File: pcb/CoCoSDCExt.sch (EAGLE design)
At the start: 47 parts, among them IC1 AM29F040J, IC2 XC9572XLVQG64, IC3 YM2413R, IC4 SN76489R, IC6 LM4558D, X1 EXPANSION_PORT_COCO, X2 EXPANSION_PORT_COCOS

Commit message: Add in YMF-262 audio IC
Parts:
- added C4.4: 50p, rcl:C-USC0402
- added C4.5, C4.6: 2n7, rcl:C-USC0402
- added C7: 10, rcl:CPOL-US140CLH-0810
- added IC10: YAC512-M, yamaha:YAC512-M
- added IC14, IC15: TL072D, linear:TL072D
- added IC9: YMF262-M, yamaha:YMF262-M
- added OSC2: 16MHz, crystal:ASE
- added R9: 33, resistor:R-US_R1206
- added U$1: (no value), coco:PROGRAM_PAK
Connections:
- new net !CE_YMF262: IC9A.!CS
- new net !IRQ_AUDIO: IC9A.!IRQ
- new net !OE: IC9A.!RD
- new net !RESET_AUDIO: IC9A.!IC
- new net AB0: IC9A.A0
- new net AB1: IC9A.A1
- new net DB0: IC9A.D0
- new net DB1: IC9A.D1
- new net DB2: IC9A.D2
- new net DB3: IC9A.D3
- new net DB4: IC9A.D4
- new net DB5: IC9A.D5
- new net DB6: IC9A.D6
- new net DB7: IC9A.D7
- new net N$10: IC10A.SMP1, IC9A.SMPAC
- new net N$11: IC10A.SMP2, IC9A.SMPBD
- new net N$12: IC9A.CLK, OSC2.OUT
- new net N$14: IC10A.SWIN, R9.2
- new net N$18: IC15B.-IN, IC15B.OUT, R9.1
- new net N$19: C4.6.1, IC10A.CH1, IC14B.+IN
- new net N$20: C4.5.1, IC10A.CH2, IC14A.+IN
- new net N$23: C4.4.1, IC10A.AOUT, IC15B.+IN
- new net N$26: IC10A.MP, IC15A.-IN, IC15A.OUT
- new net N$28: C7.+, IC10A.CV, IC15A.+IN
- new net N$6: IC10A.CLK, IC9A.SY
- new net N$7: IC10A.DIN, IC9A.DOAB
- new net YMF_CH_0: IC14B.-IN, IC14B.OUT
- new net YMF_CH_1: IC14A.-IN, IC14A.OUT
- net !WE: now also IC9A.!WR
- net +3V3: now also OSC2.VDD
- net +5V: now also IC10A.FSEL, IC10A.TEST1
- net GND: now also C4.4.2, C4.5.2, C4.6.2, C7.-, OSC2.GND

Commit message: Initial fitment
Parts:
- removed C1.2, C3.1, C4.1: .1, resistor:C-USC0402
- removed C10, C11, C2: .1, resistor:C-EUC1206
- removed C14, C16, C3: .0015, resistor:C-EUC1206
- removed C4: 10, resistor:C-USC0805
- removed C5: 1/50, resistor:C-USC0805
- removed IC3: YM2413R, yamaha:YM2413R
- removed IC4: SN76489R, texas-instruments:SN76489R
- removed IC6: LM4558D, op-amps-jlb:LM4558D
- removed OSC2: 16MHz, crystal:ASE
- removed R1: 10K, resistor:R-US_R0402
- removed R2, R38, R39: 10K, rcl:R-US_R1206
- removed R3, R4, R5: 4K7, rcl:R-US_R1206
- removed R40: 16K, rcl:R-US_R1206
- removed R41: 1.3K (1%), rcl:R-US_R0402
- removed R42: 1k (1%), rcl:R-US_R0402
- removed R6, R7, R8: 2K2, rcl:R-US_R1206
- added C10.1, C14.1, C15.1, C15.2, C9.1: .1, rcl:C-USC0402
- added C17, C18, C19, C20: (no value), cap-pan40:C-BP-SMD-SV-B
- added C4.2: 10u, rcl:C-USC0402
- added R10, R11: 2K, resistor:R-US_R1206
- added R12, R13: 10K, resistor:R-US_R1206
- added R14, R15: 10K, resistor:R-US_R0402
- added R16: ?K, resistor:R-US_R1206
- added SV1: (no value), con-lstb-rp:MA03-1
- C7: value 10 -> (none); device rcl:CPOL-US140CLH-0810 -> cap-pan40:C-BP-SMD-SV-B
- IC14, IC15: value TL072D -> TL974; device linear:TL072D -> linear-jlb:TL974
- OSC1: value ASE -> 16MHz
- R9: device resistor:R-US_R1206 -> resistor:R-US_R0402
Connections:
- removed net CH0: IC3A.RO, R3.2, R6.1
- removed net CH1: IC3A.MO, R4.2, R7.1
- removed net N$1: C10.1, C14.1, R3.1
- removed net N$2: C2.1, R2.2
- removed net N$3: IC6A.-IN, R2.1, R38.1, R39.1, R40.2
- removed net N$4: C11.2, C16.1, R4.1
- removed net N$49: C10.2, R38.2
- removed net N$5: C2.2, C3.1, R5.1
- removed net N$50: C11.1, R39.2
- removed net N$52: IC6A.+IN, IC6B.-IN, IC6B.OUT
- removed net N$54: C5.1, IC6A.OUT, R40.1
- removed net N$55: C4.1, IC6B.+IN, R41.1, R42.2
- removed net N$8: IC2.FB1MC9-I/O/GCK1, OSC1.OUT
- new net AUDIO_L: C7.1, SV1.1
- new net AUDIO_R: C18.1, SV1.3
- new net N$13: C18.2, C19.2, R11.1
- new net N$15: C17.1, R12.2
- new net N$16: C19.1, R13.2
- new net N$17: IC15B.-IN, R12.1, R13.1, R16.2
- new net N$21: IC15A.-IN, IC15A.OUT, IC15B.+IN
- new net N$24: C15.2.1, IC15A.+IN, R14.2, R15.1
- new net N$27: C20.2, IC15B.OUT, R16.1
- new net N$9: C17.2, C7.2, R10.1
- net !CE_SN: no longer IC4A.!CE
- net !CE_YM: no longer IC3A.!CS
- net !RESET_YM: no longer IC3A.!RESET
- net !WE_SN: no longer IC4A.!WE
- net +3V3: no longer C1.2.1, OSC2.VDD
- net +5V: now also C10.1.1, C14.1.1, C15.1.1, C9.1.1, IC10P.VCC, IC10P.VCC@1, IC14G$1.V+, IC15G$1.V+, IC9P.VCC, R14.1; no longer C3.1.1, C4.1.1, IC3P.VCC, IC4P.VCC, IC6P.V+, R1.2, R42.1
- net A0_YM: no longer IC3A.!A0
- net BD0: no longer IC4A.D0
- net BD1: no longer IC4A.D1
- net BD2: no longer IC4A.D2
- net BD3: no longer IC4A.D3
- net BD4: no longer IC4A.D4
- net BD5: no longer IC4A.D5
- net BD6: no longer IC4A.D6
- net BD7: no longer IC4A.D7
- net CH2: no longer IC4A.AUDIO, R5.2, R8.1
- net CLK_SN: no longer IC4A.CLOCK
- net CLK_YM: no longer IC3A.XIN
- net D0: no longer IC3A.D0
- net D1: no longer IC3A.D1
- net D2: no longer IC3A.D2
- net D3: no longer IC3A.D3
- net D4: no longer IC3A.D4
- net D5: no longer IC3A.D5
- net D6: no longer IC3A.D6
- net D7: no longer IC3A.D7
- net GND: now also C10.1.2, C14.1.2, C15.1.2, C15.2.2, C4.2.2, C9.1.2, IC10P.GND, IC14G$1.V-, IC15G$1.V-, IC9P.GND, R15.2, SV1.2; no longer C1.2.2, C14.2, C16.2, C3.1.2, C3.2, C4.1.2, C4.2, C7.-, IC3A.!WE, IC3P.GND, IC4P.GND, IC6P.V-, OSC2.GND, R41.2, R6.2, R7.2, R8.2
- net N$12: now also OSC1.OUT; no longer OSC2.OUT
- net N$18: now also IC14D.-IN, IC14D.OUT; no longer IC15B.-IN, IC15B.OUT
- net N$23: now also IC14D.+IN; no longer IC15B.+IN
- net N$26: now also IC14C.-IN, IC14C.OUT; no longer IC15A.-IN, IC15A.OUT
- net N$28: now also C4.2.1, IC14C.+IN; no longer C7.+, IC15A.+IN
- net READY: no longer IC4A.READY, R1.1
- net SND: now also C20.1; no longer C5.2
- net YMF_CH_0: now also R10.2
- net YMF_CH_1: now also R11.2
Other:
- moved on the sheet: IC15A, IC15B

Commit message: More fitment positioning
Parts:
- C4.2: device rcl:C-USC0402 -> rcl:C-USC0805
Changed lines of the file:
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@@
 <part name="GND36" library="supply1" deviceset="GND" device=""/>
 <part name="GND39" library="supply1" deviceset="GND" device=""/>
-<part name="C4.2" library="rcl" deviceset="C-US" device="C0402" value="10u"/>
+<part name="C4.2" library="rcl" deviceset="C-US" device="C0805" value="10u"/>
 <part name="C7" library="cap-pan40" deviceset="C-BP" device="-SMD-SV-B"/>
 <part name="C17" library="cap-pan40" deviceset="C-BP" device="-SMD-SV-B"/>

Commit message: positioning
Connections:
- net N$18: now also IC14A.-IN, IC14A.OUT; no longer IC14D.-IN, IC14D.OUT
- net N$19: now also IC14D.+IN; no longer IC14B.+IN
- net N$20: now also IC14C.+IN; no longer IC14A.+IN
- net N$23: now also IC14A.+IN; no longer IC14D.+IN
- net N$26: now also IC14B.-IN, IC14B.OUT; no longer IC14C.-IN, IC14C.OUT
- net N$28: now also IC14B.+IN; no longer IC14C.+IN
- net YMF_CH_0: now also IC14D.-IN, IC14D.OUT; no longer IC14B.-IN, IC14B.OUT
- net YMF_CH_1: now also IC14C.-IN, IC14C.OUT; no longer IC14A.-IN, IC14A.OUT
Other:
- moved on the sheet: IC14A, IC14B, IC14C, IC14D
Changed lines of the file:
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@@
 <instance part="C19" gate="G$1" x="134.62" y="58.42" rot="R90"/>
 <instance part="C20" gate="G$1" x="220.98" y="68.58" rot="R90"/>
-<instance part="IC14" gate="A" x="203.2" y="182.88"/>
-<instance part="IC14" gate="B" x="203.2" y="198.12"/>
-<instance part="IC14" gate="C" x="203.2" y="152.4"/>
-<instance part="IC14" gate="D" x="203.2" y="167.64"/>
+<instance part="IC14" gate="C" x="203.2" y="182.88"/>
+<instance part="IC14" gate="D" x="203.2" y="198.12"/>
+<instance part="IC14" gate="B" x="203.2" y="152.4"/>
+<instance part="IC14" gate="A" x="203.2" y="167.64"/>
 <instance part="IC15" gate="A" x="185.42" y="78.74"/>
 <instance part="IC15" gate="B" x="205.74" y="68.58"/>
@@
 <wire x1="175.26" y1="154.94" x2="175.26" y2="182.88" width="0.1524" layer="91"/>
 <junction x="175.26" y="182.88"/>
-<pinref part="IC14" gate="B" pin="+IN"/>
+<pinref part="IC14" gate="D" pin="+IN"/>
 </segment>
 </net>
@@
 <wire x1="167.64" y1="154.94" x2="167.64" y2="177.8" width="0.1524" layer="91"/>
 <junction x="167.64" y="177.8"/>
-<pinref part="IC14" gate="A" pin="+IN"/>
+<pinref part="IC14" gate="C" pin="+IN"/>
 </segment>
 </net>
@@
 <junction x="215.9" y="182.88"/>
 <label x="218.44" y="182.88" size="1.27" layer="95" xref="yes"/>
-<pinref part="IC14" gate="A" pin="-IN"/>
-<pinref part="IC14" gate="A" pin="OUT"/>
+<pinref part="IC14" gate="C" pin="-IN"/>
+<pinref part="IC14" gate="C" pin="OUT"/>
 </segment>
 <segment>
@@
 <wire x1="215.9" y1="160.02" x2="215.9" y2="167.64" width="0.1524" layer="91"/>
 <wire x1="215.9" y1="167.64" x2="210.82" y2="167.64" width="0.1524" layer="91"/>
-<pinref part="IC14" gate="D" pin="-IN"/>
-<pinref part="IC14" gate="D" pin="OUT"/>
+<pinref part="IC14" gate="A" pin="-IN"/>
+<pinref part="IC14" gate="A" pin="OUT"/>
 </segment>
 </net>
@@
 <wire x1="160.02" y1="167.64" x2="190.5" y2="167.64" width="0.1524" layer="91"/>
 <wire x1="190.5" y1="167.64" x2="190.5" y2="170.18" width="0.1524" layer="91"/>
-<pinref part="IC14" gate="D" pin="+IN"/>
+<pinref part="IC14" gate="A" pin="+IN"/>
 </segment>
 </net>
@@
 <wire x1="190.5" y1="149.86" x2="193.04" y2="149.86" width="0.1524" layer="91"/>
 <junction x="193.04" y="149.86"/>
-<pinref part="IC14" gate="C" pin="-IN"/>
-<pinref part="IC14" gate="C" pin="OUT"/>
+<pinref part="IC14" gate="B" pin="-IN"/>
+<pinref part="IC14" gate="B" pin="OUT"/>
 </segment>
 </net>
@@
 <junction x="152.4" y="157.48"/>
 <pinref part="C4.2" gate="G$1" pin="1"/>
-<pinref part="IC14" gate="C" pin="+IN"/>
+<pinref part="IC14" gate="B" pin="+IN"/>
 </segment>
 </net>
@@
 <junction x="215.9" y="198.12"/>
 <label x="218.44" y="198.12" size="1.27" layer="95" xref="yes"/>
-<pinref part="IC14" gate="B" pin="-IN"/>
-<pinref part="IC14" gate="B" pin="OUT"/>
-</segment>
-<segment>
+<pinref part="IC14" gate="D" pin="-IN"/>
+<pinref part="IC14" gate="D" pin="OUT"/>
+</segment>
+<segment>

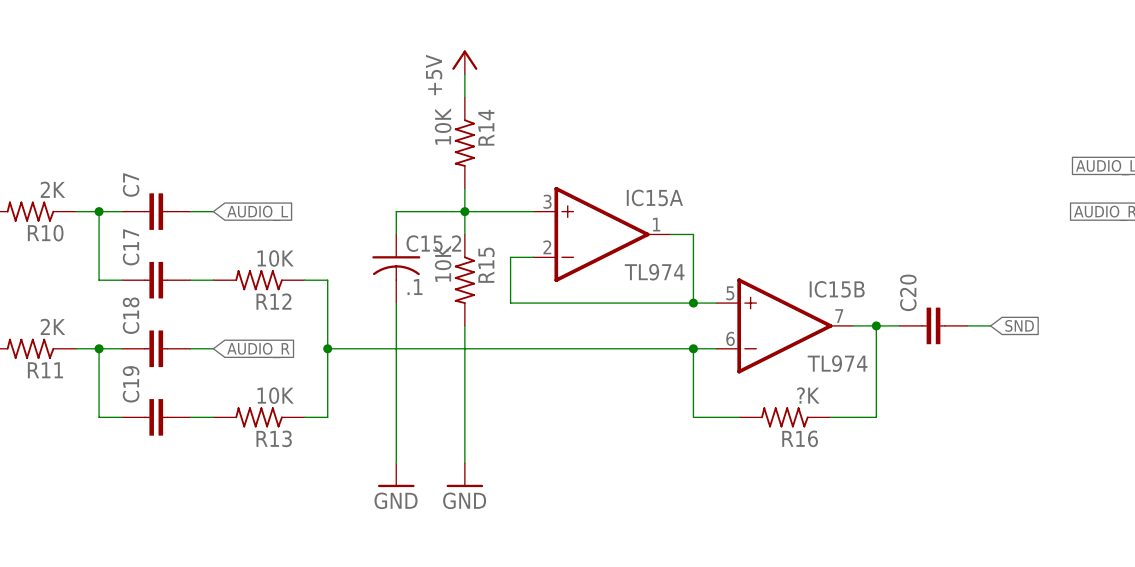
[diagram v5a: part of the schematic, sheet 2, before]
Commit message: Extending PCB to support tabs
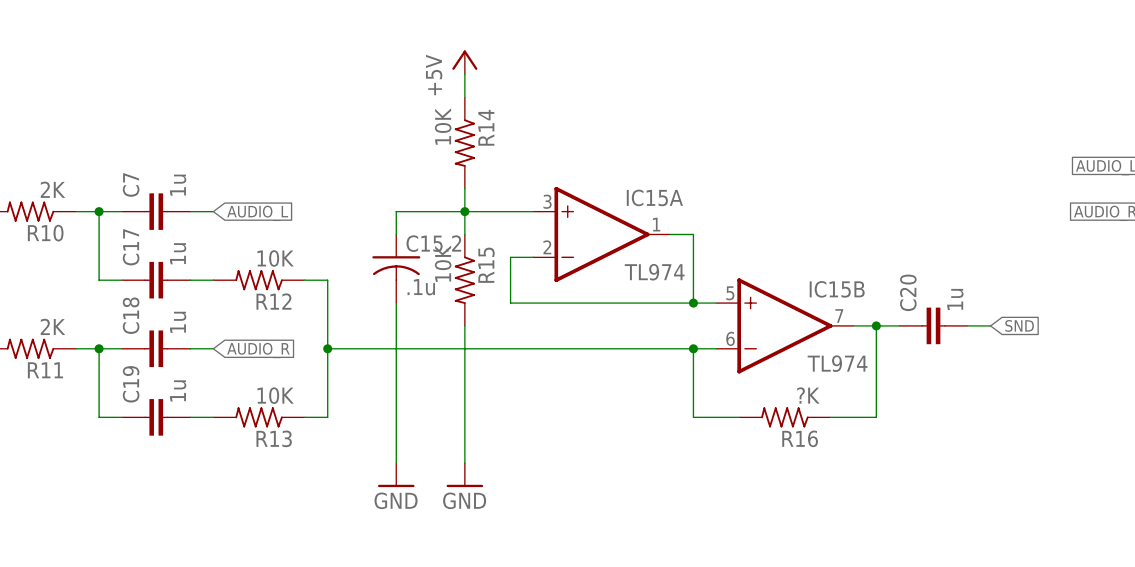
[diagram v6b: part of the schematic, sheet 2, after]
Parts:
- C15.2: value .1 -> .1u
- C17, C18, C19, C20, C7: value (none) -> 1u
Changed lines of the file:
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@@
 <part name="P+13" library="supply1" deviceset="+5V" device=""/>
 <part name="GND32" library="supply1" deviceset="GND" device=""/>
-<part name="C15.2" library="rcl" deviceset="C-US" device="C0402" value=".1"/>
+<part name="C15.2" library="rcl" deviceset="C-US" device="C0402" value=".1u"/>
 <part name="GND34" library="supply1" deviceset="GND" device=""/>
 <part name="R16" library="resistor" deviceset="R-US_" device="R1206" value="?K"/>
@@
 <part name="GND39" library="supply1" deviceset="GND" device=""/>
 <part name="C4.2" library="rcl" deviceset="C-US" device="C0805" value="10u"/>
-<part name="C7" library="cap-pan40" deviceset="C-BP" device="-SMD-SV-B"/>
-<part name="C17" library="cap-pan40" deviceset="C-BP" device="-SMD-SV-B"/>
-<part name="C18" library="cap-pan40" deviceset="C-BP" device="-SMD-SV-B"/>
-<part name="C19" library="cap-pan40" deviceset="C-BP" device="-SMD-SV-B"/>
-<part name="C20" library="cap-pan40" deviceset="C-BP" device="-SMD-SV-B"/>
+<part name="C7" library="cap-pan40" deviceset="C-BP" device="-SMD-SV-B" value="1u"/>
+<part name="C17" library="cap-pan40" deviceset="C-BP" device="-SMD-SV-B" value="1u"/>
+<part name="C18" library="cap-pan40" deviceset="C-BP" device="-SMD-SV-B" value="1u"/>
+<part name="C19" library="cap-pan40" deviceset="C-BP" device="-SMD-SV-B" value="1u"/>
+<part name="C20" library="cap-pan40" deviceset="C-BP" device="-SMD-SV-B" value="1u"/>
 <part name="IC14" library="linear-jlb" deviceset="TL974" device=""/>
 <part name="IC15" library="linear-jlb" deviceset="TL974" device=""/>

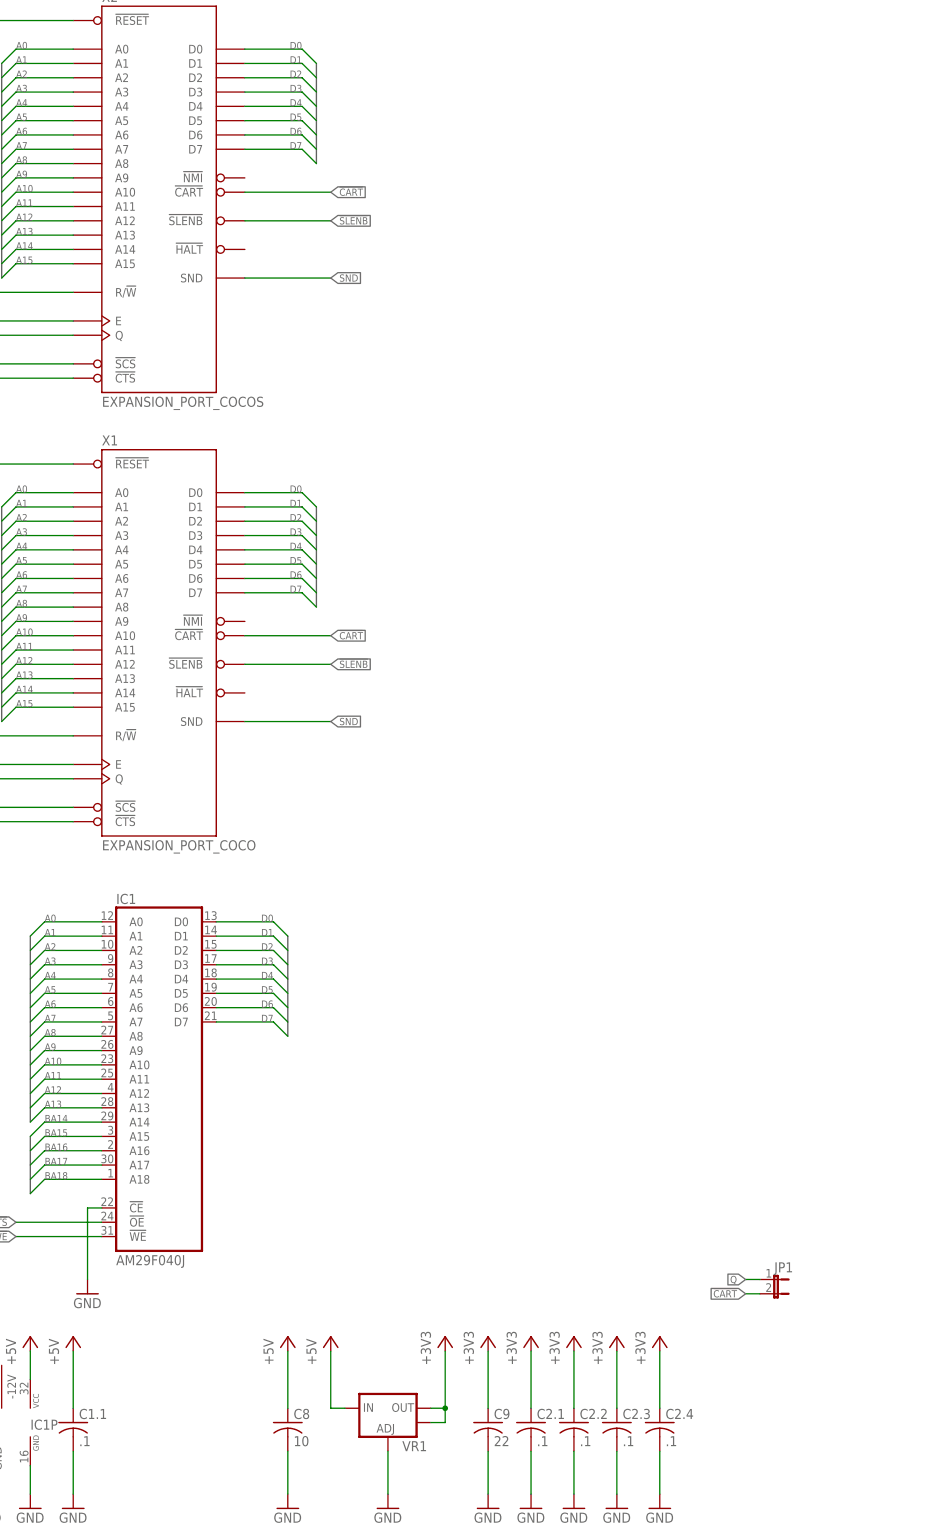
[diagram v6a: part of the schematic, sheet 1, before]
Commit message: routing pass-thru connector
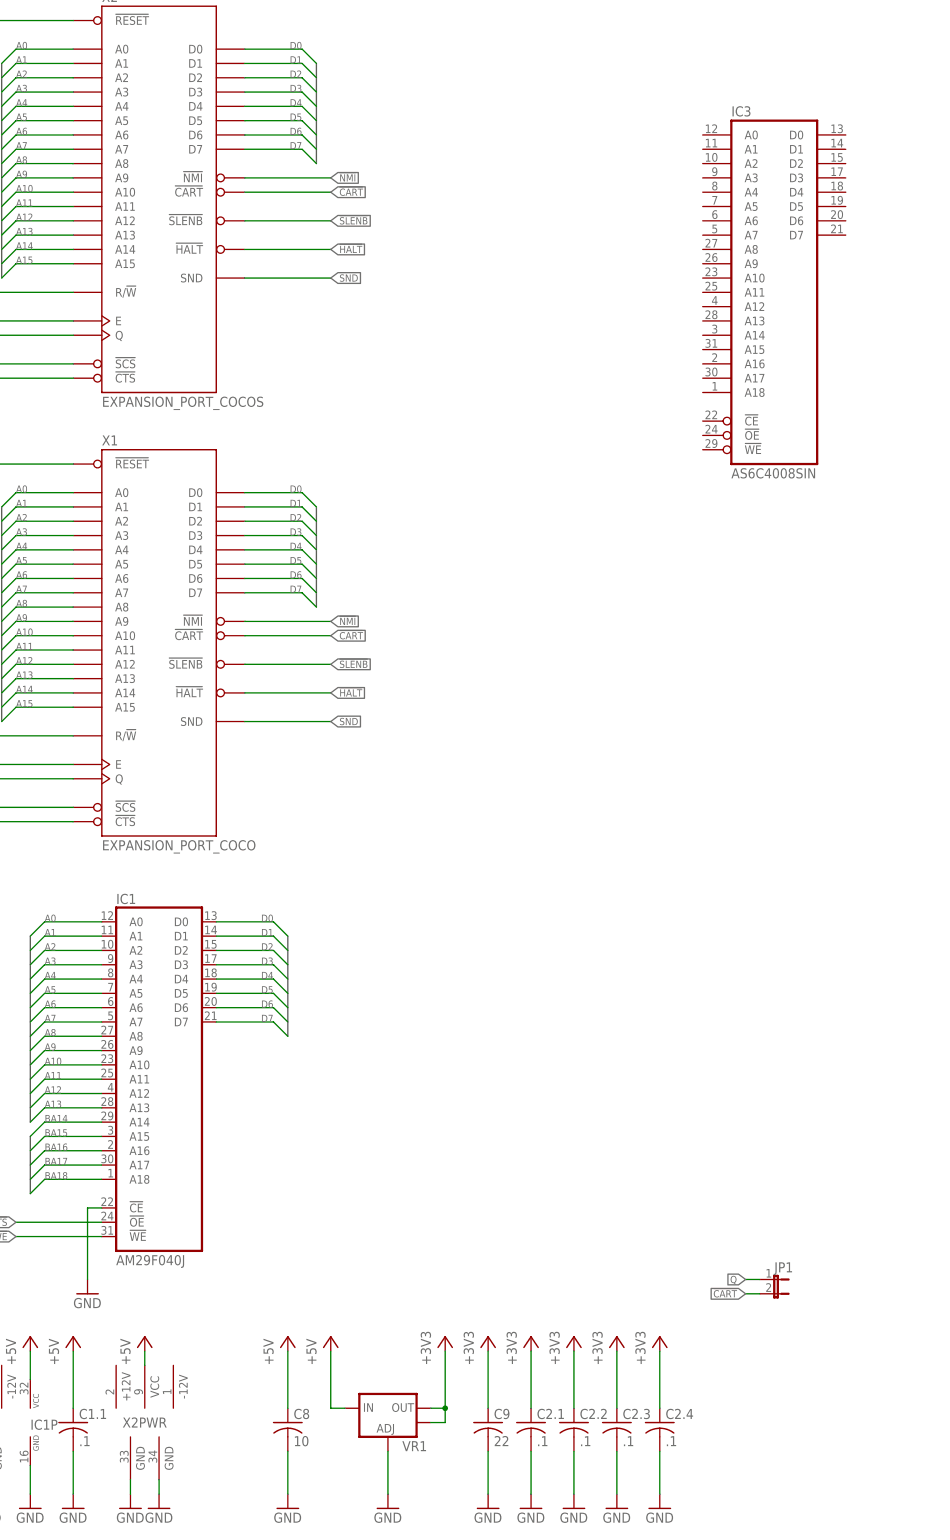
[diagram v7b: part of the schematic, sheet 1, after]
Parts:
- added IC3: AS6C4008SIN, memory-alliance:AS6C4008SIN
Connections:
- new net !HALT: X1X.!HALT, X2X.!HALT
- new net !NMI: X1X.!NMI, X2X.!NMI
- net +5V: now also X2PWR.VCC
- net GND: now also X2PWR.GND@1, X2PWR.GND@2
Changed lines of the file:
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@@
 <part name="IC14" library="linear-jlb" deviceset="TL974" device=""/>
 <part name="IC15" library="linear-jlb" deviceset="TL974" device=""/>
+<part name="P+4" library="supply1" deviceset="+5V" device=""/>
+<part name="GND9" library="supply1" deviceset="GND" device=""/>
+<part name="GND10" library="supply1" deviceset="GND" device=""/>
+<part name="IC3" library="memory-alliance" deviceset="AS6C4008" device="SIN"/>
 </parts>
 <sheets>
@@
 <instance part="X2" gate="X" x="121.92" y="177.8"/>
 <instance part="U$1" gate="A" x="388.62" y="-48.26"/>
+<instance part="X2" gate="PWR" x="119.38" y="-38.1"/>
+<instance part="P+4" gate="1" x="119.38" y="-22.86"/>
+<instance part="GND9" gate="1" x="116.84" y="-53.34"/>
+<instance part="GND10" gate="1" x="121.92" y="-53.34"/>
+<instance part="IC3" gate="A" x="231.14" y="162.56"/>
 </instances>
 <busses>
@@
 <pinref part="C8" gate="G$1" pin="1"/>
 <wire x1="144.78" y1="-25.4" x2="144.78" y2="-35.56" width="0.1524" layer="91"/>
+</segment>
+<segment>
+<pinref part="P+4" gate="1" pin="+5V"/>
+<pinref part="X2" gate="PWR" pin="VCC"/>
+<wire x1="119.38" y1="-25.4" x2="119.38" y2="-27.94" width="0.1524" layer="91"/>
 </segment>
 </net>
@@
 <wire x1="144.78" y1="-43.18" x2="144.78" y2="-50.8" width="0.1524" layer="91"/>
 </segment>
+<segment>
+<pinref part="GND9" gate="1" pin="GND"/>
+<pinref part="X2" gate="PWR" pin="GND@1"/>
+<wire x1="116.84" y1="-50.8" x2="116.84" y2="-48.26" width="0.1524" layer="91"/>
+</segment>
+<segment>
+<pinref part="X2" gate="PWR" pin="GND@2"/>
+<pinref part="GND10" gate="1" pin="GND"/>
+<wire x1="121.92" y1="-48.26" x2="121.92" y2="-50.8" width="0.1524" layer="91"/>
+</segment>
 </net>
 <net name="R/!W" class="0">
@@
 </segment>
 </net>
+<net name="!NMI" class="0">
+<segment>
+<pinref part="X2" gate="X" pin="!NMI"/>
+<wire x1="137.16" y1="182.88" x2="152.4" y2="182.88" width="0.1524" layer="91"/>
+<label x="152.4" y="182.88" size="1.27" layer="95" xref="yes"/>
+</segment>
+<segment>
+<pinref part="X1" gate="X" pin="!NMI"/>
+<wire x1="137.16" y1="104.14" x2="152.4" y2="104.14" width="0.1524" layer="91"/>
+<label x="152.4" y="104.14" size="1.27" layer="95" xref="yes"/>
+</segment>
+</net>
+<net name="!HALT" class="0">
+<segment>
+<pinref part="X2" gate="X" pin="!HALT"/>
+<wire x1="137.16" y1="170.18" x2="152.4" y2="170.18" width="0.1524" layer="91"/>
+<label x="152.4" y="170.18" size="1.27" layer="95" xref="yes"/>
+</segment>
+<segment>
+<pinref part="X1" gate="X" pin="!HALT"/>
+<wire x1="137.16" y1="91.44" x2="152.4" y2="91.44" width="0.1524" layer="91"/>
+<label x="152.4" y="91.44" size="1.27" layer="95" xref="yes"/>
+</segment>
+</net>
